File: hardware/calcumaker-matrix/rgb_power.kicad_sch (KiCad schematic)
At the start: 15 parts, among them J2 VSYS IN (LED pwr), Q1 AO3401A, Q2 2N7002, U4 74LVC1G125, U5 74LVC1G125, U6 74LVC1G125

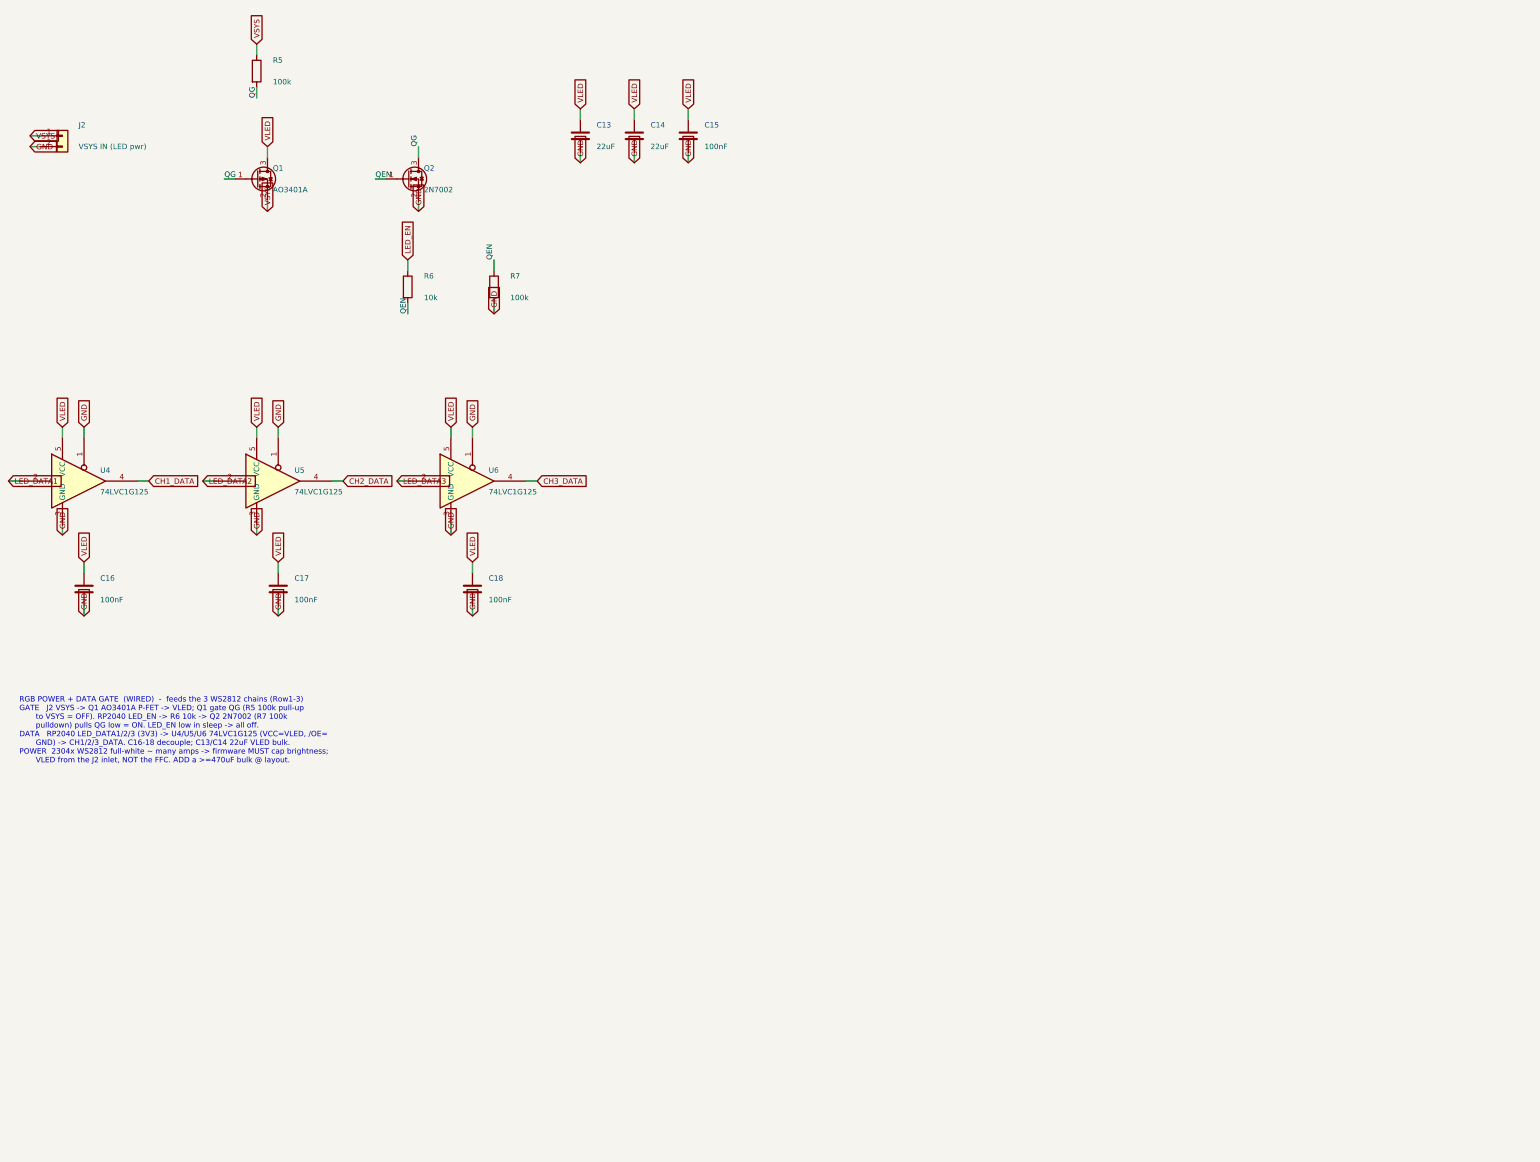
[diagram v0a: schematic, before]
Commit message: Floorplan both display PCBs and verify their schematic nets
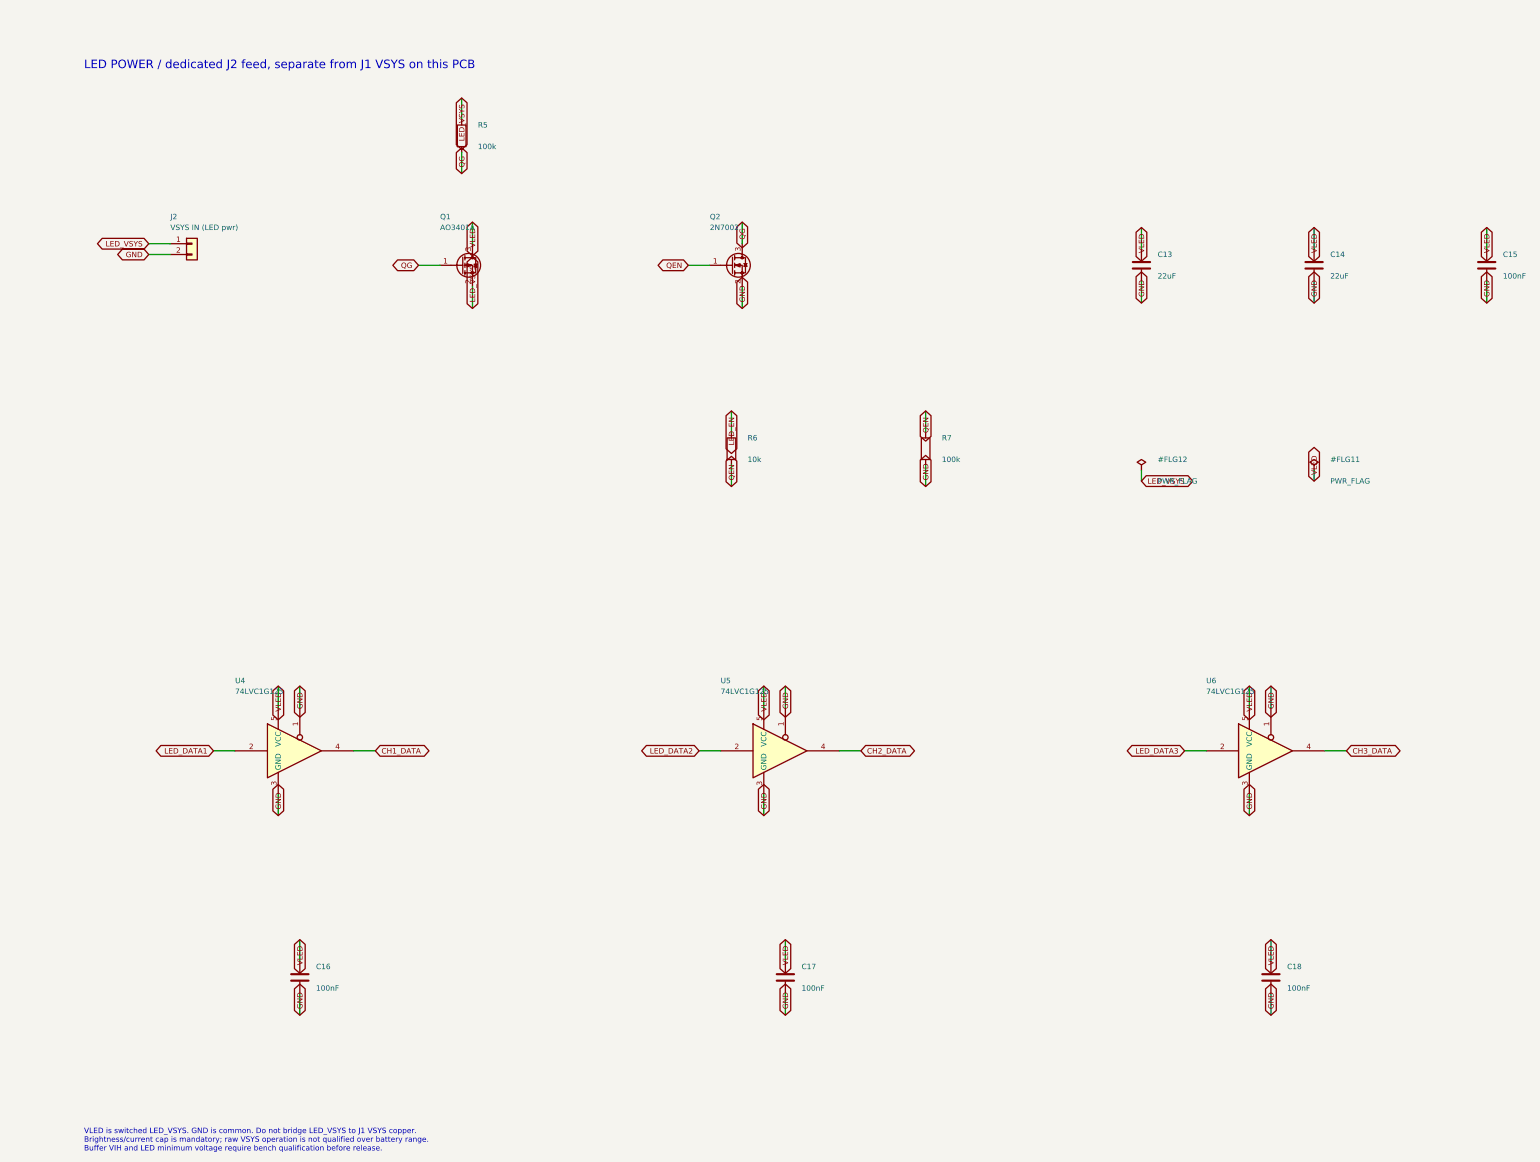
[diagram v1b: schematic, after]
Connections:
- net VSYS renamed LED_VSYS
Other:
- note added: "LED POWER / dedicated J2 feed, separate from J1 VSYS on this PCB"
- note added: "VLED is switched LED_VSYS. GND is common. Do not bridge LED_VSYS to J1 VSYS copper. Brightness/current cap is mandatory; raw VSYS operation is not qualified over battery range. Buffer VIH and LED minimum voltage require bench qualification before release."
- note removed: "RGB POWER + DATA GATE (WIRED) - feeds the 3 WS2812 chains (Row1-3) GATE J2 VSYS -> Q1 AO3401A P-FET -> VLED; Q1 gate QG (R5 100k pull-up to VSYS = OFF). RP2040 LED_EN -> R6 10k -> Q2 2N7002 (R7 100k pulldown) pulls QG low = ON. LED_EN low in sleep -> all off. DATA RP2040 LED_DATA1/2/3 (3V3) -> U4/U5/U6 74LVC1G125 (VCC=VLED, /OE= GND) -> CH1/2/3_DATA. C16-18 decouple; C13/C14 22uF VLED bulk. POWER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"
- title: Calcumaker 16 — RGB Matrix — RGB power + data gate (load switch + 3x level shift) -> Calcumaker 16 / matrix / rgb power
- moved on the sheet: C13, C14, C15, C16, C17, C18, J2, Q1, Q2, R5, R6, R7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
